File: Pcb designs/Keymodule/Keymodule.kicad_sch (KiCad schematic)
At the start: 109 parts, among them J1 Conn_01x01, J11 USB connect, J2 Conn_01x01, J3 Conn_01x03, J4 Conn_01x01, J5 Conn_01x01, J6 Conn_01x03, U1 RP2040, U2 SN74LV1T34DBV, U3 AMS1117-3.3, U4 W25Q128JVS, Y1 ABM8-272-T3

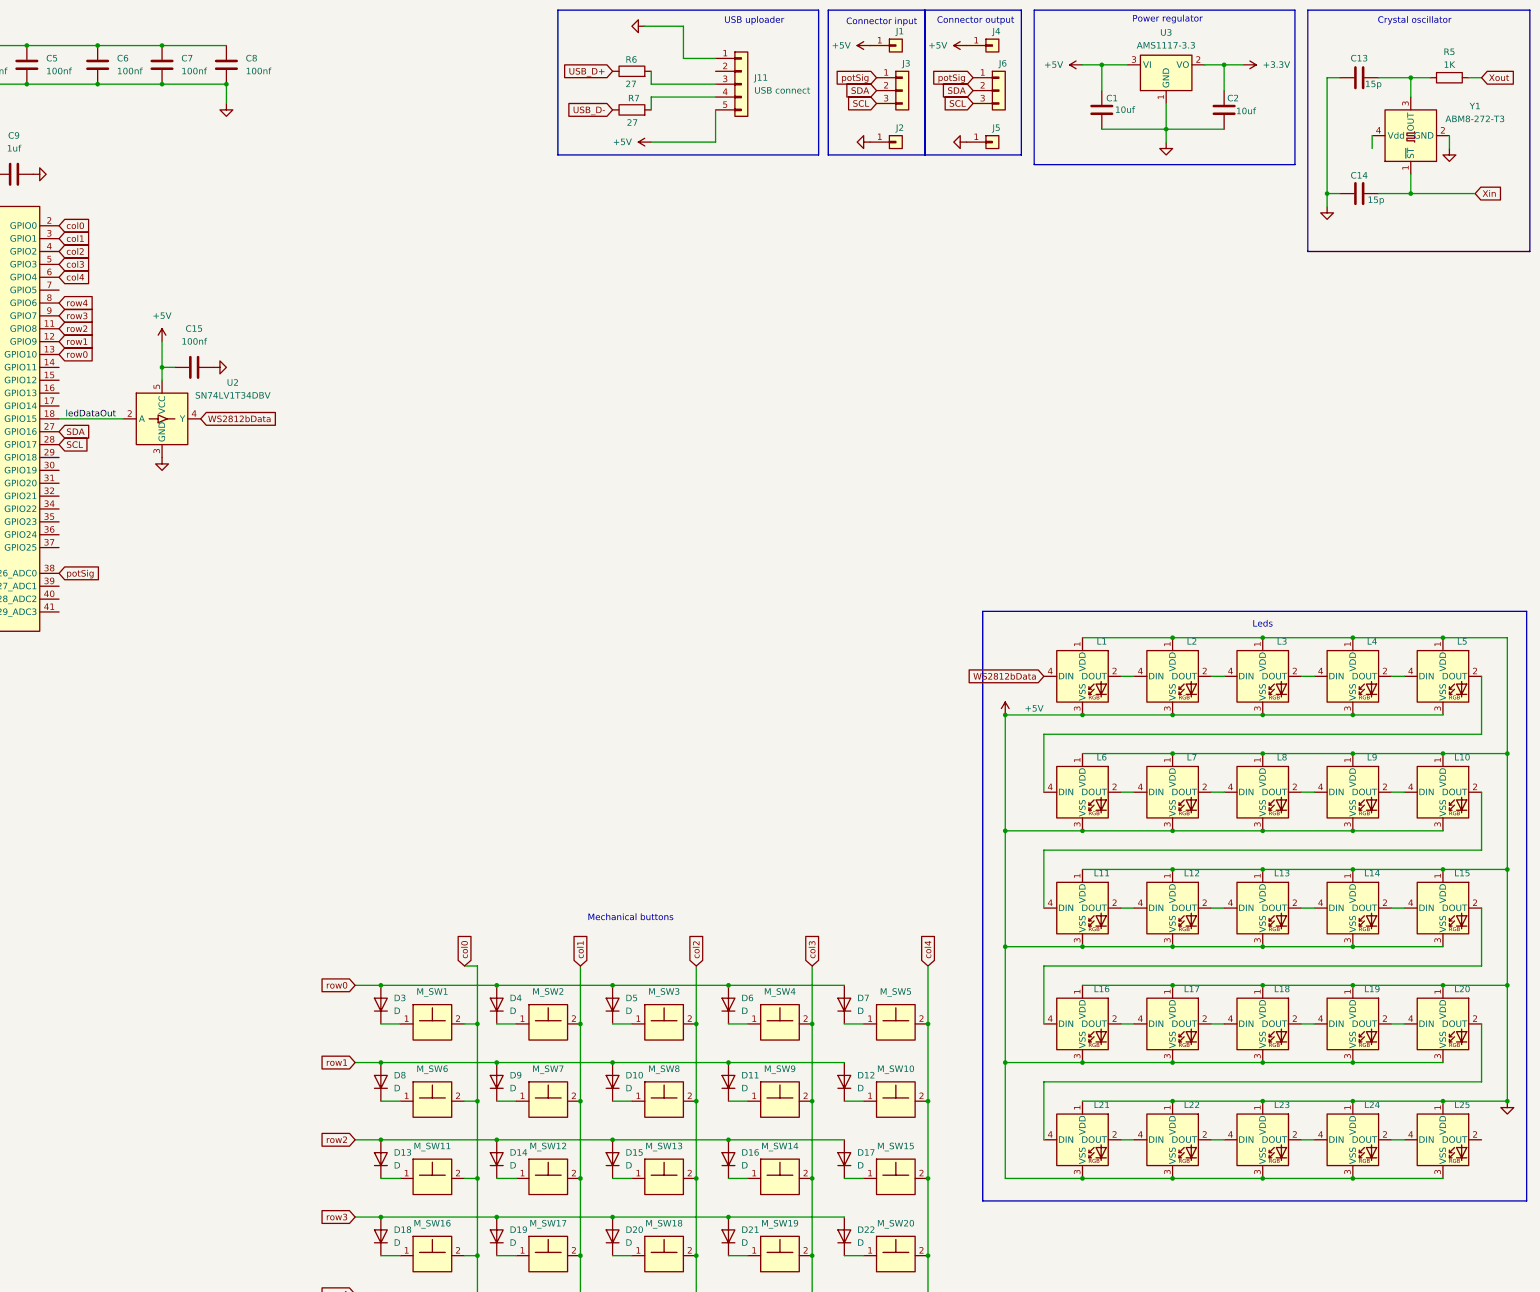
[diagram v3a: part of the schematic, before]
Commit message: Led's & buttons are done
Still need to optimize and check MCU connections
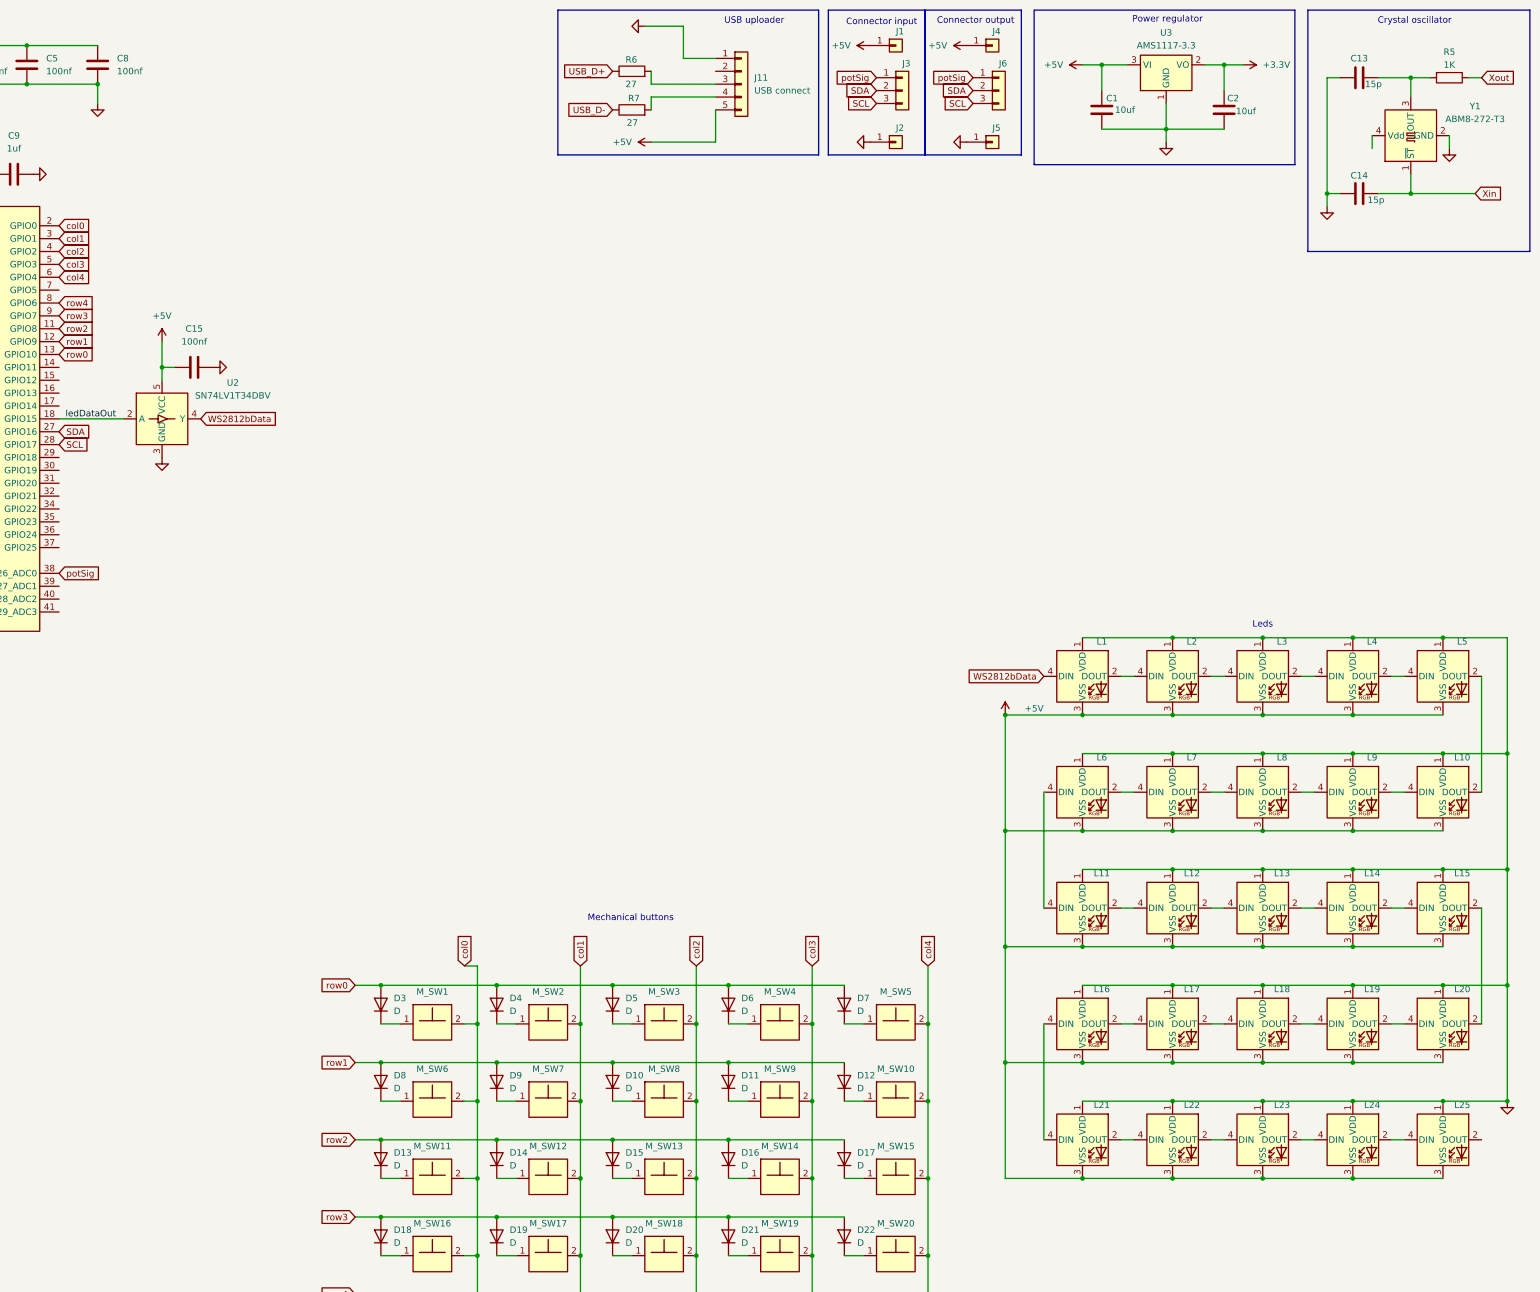
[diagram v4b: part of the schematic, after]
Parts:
- removed C6, C7: 100nf, Capacitor_SMD:C_0402_1005Metric, symbol Device:C
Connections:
- net at L6.4 (DIN): now also L11.4 (DIN); no longer L5.2 (DOUT)
- net at L10.2 (DOUT): now also L5.2 (DOUT); no longer L11.4 (DIN)
- net at L21.4 (DIN): now also L16.4 (DIN); no longer L20.2 (DOUT)
- net at L15.2 (DOUT): now also L20.2 (DOUT); no longer L16.4 (DIN)
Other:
- moved on the sheet: C8

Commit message: Better final version
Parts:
- J3, J6: footprint Connector_PinHeader_1.27mm:PinHeader_1x03_P1.27mm_Horizontal -> Connector_PinHeader_2.54mm:PinHeader_1x03_P2.54mm_Horizontal
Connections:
- net potSig: now also U1.37 (GPIO25)
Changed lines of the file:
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@@
 	(wire
 		(pts
+			(xy 115.57 120.65) (xy 115.57 125.73)
+		)
+		(stroke
+			(width 0)
+			(type default)
+		)
+	)
+	(wire
+		(pts
 			(xy 24.13 60.96) (xy 24.13 58.42)
 		)
@@
 			)
 		)
-		(property "Footprint" "Connector_PinHeader_1.27mm:PinHeader_1x03_P1.27mm_Horizontal"
+		(property "Footprint" "Connector_PinHeader_2.54mm:PinHeader_1x03_P2.54mm_Horizontal"
 			(at 300.99 30.48 0)
 			(effects
@@
 			)
 		)
-		(property "Footprint" "Connector_PinHeader_1.27mm:PinHeader_1x03_P1.27mm_Horizontal"
+		(property "Footprint" "Connector_PinHeader_2.54mm:PinHeader_1x03_P2.54mm_Horizontal"
 			(at 281.94 30.48 0)
 			(effects

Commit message: Ihope this is the one
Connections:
- net col0: now also U1.8 (GPIO6); no longer U1.2 (GPIO0)
- net col1: now also U1.4 (GPIO2); no longer U1.3 (GPIO1)
- net col2: now also U1.11 (GPIO8); no longer U1.4 (GPIO2)
- net col3: now also U1.12 (GPIO9); no longer U1.5 (GPIO3)
- net col4: now also U1.13 (GPIO10); no longer U1.6 (GPIO4)
- net row0: now also U1.3 (GPIO1); no longer U1.13 (GPIO10)
- net row1: now also U1.2 (GPIO0); no longer U1.12 (GPIO9)
- net row2: now also U1.5 (GPIO3); no longer U1.11 (GPIO8)
- net row3: now also U1.6 (GPIO4); no longer U1.9 (GPIO7)
- net row4: now also U1.9 (GPIO7); no longer U1.8 (GPIO6)
